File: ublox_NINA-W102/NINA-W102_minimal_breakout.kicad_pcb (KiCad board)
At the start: 2 copper layers, 16 parts, among them J1 Conn_01x15, J2 Conn_01x15, J3 6_PIN_SERIAL_TARGETLOCK, SW1 BOOT, SW2 RESET, U1 NINA-W102

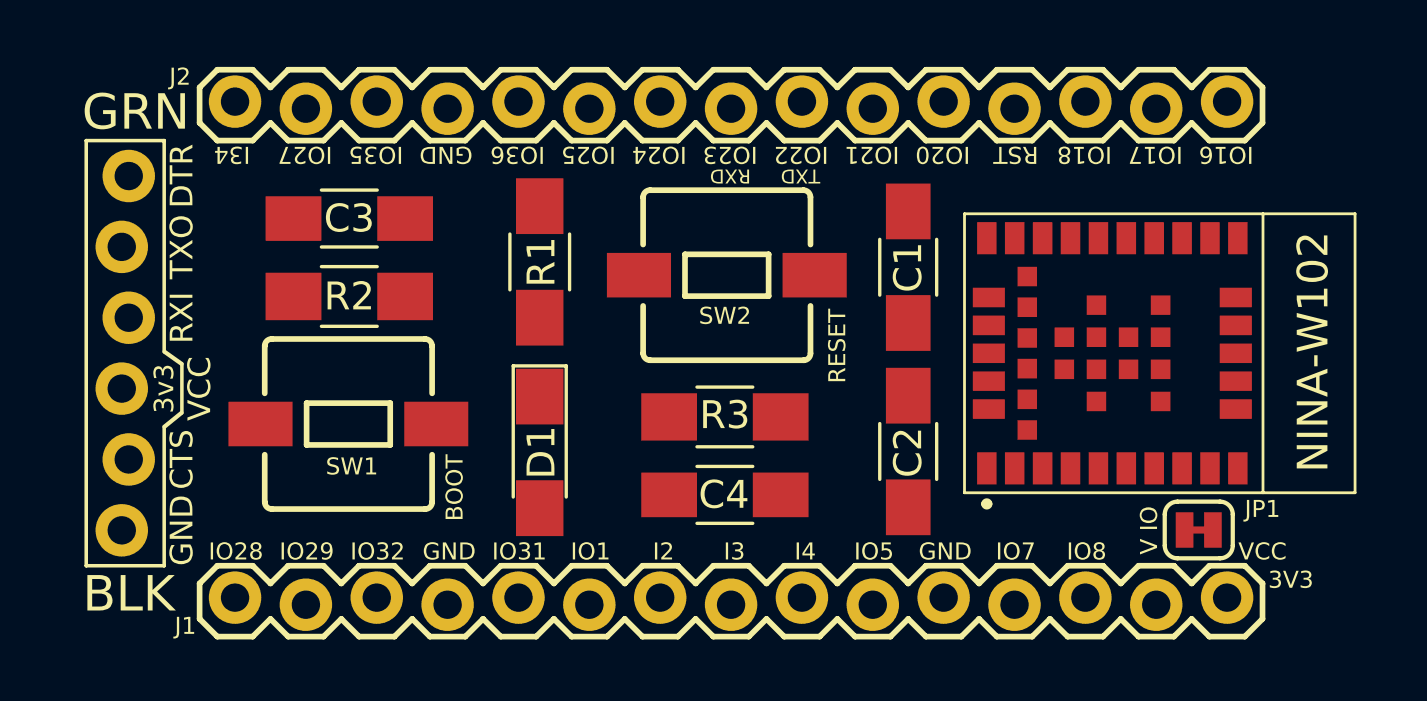
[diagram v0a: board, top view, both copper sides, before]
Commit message: First routing done
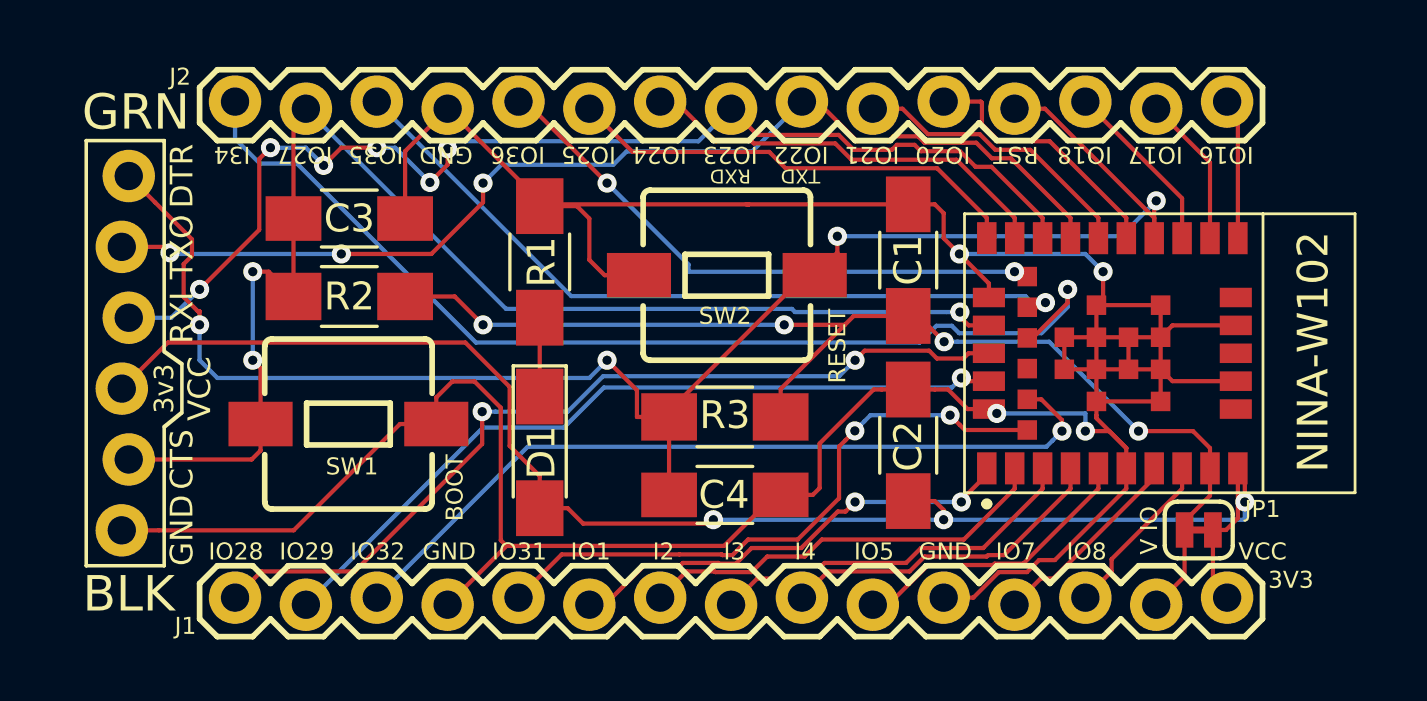
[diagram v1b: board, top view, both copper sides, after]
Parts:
- moved C1 0.25 mm to (134.6, 103.1)
- moved C2 0.22 mm to (134.6, 109.7)
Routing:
- net GND: track 0.00 -> 129.4 mm, vias 0 -> 4
- net DTR: track 0.00 -> 59.4 mm, vias 0 -> 4
- net +3V3: track 0.00 -> 55.1 mm, vias 0 -> 3
- net CTS: track 0.00 -> 47.9 mm, vias 0 -> 3
- net +1V8: track 0.00 -> 42.0 mm, vias 0 -> 4
- net RXD: track 0.00 -> 41.7 mm, vias 0 -> 6
- net TXD: track 0.00 -> 39.4 mm, vias 0 -> 3
- net Net-(J2-Pad1): track 0.00 -> 38.0 mm, vias 0 -> 1
- net Net-(J1-Pad1): track 0.00 -> 31.6 mm, vias 0 -> 2
- net Net-(J1-Pad3): track 0.00 -> 29.0 mm, vias 0 -> 1
- net Net-(J1-Pad2): track 0.00 -> 27.9 mm, vias 0 -> 1
- net Net-(J2-Pad3): track 0.00 -> 27.7 mm, vias 0 -> 1
- net Net-(J1-Pad5): track 0.00 -> 22.3 mm, vias 0 -> 2
- net Net-(J2-Pad5): track 0.00 -> 21.0 mm, vias 0 -> 2
- net Net-(J2-Pad6): track 0.00 -> 16.6 mm
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
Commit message: First try with groundplane
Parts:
- moved ? 10.5 mm to (83.7, 106.3)
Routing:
- added copper zone on B.Cu, net GND
- added copper zone on F.Cu, net GND
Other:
- board outline added: 47 x 20.7 mm

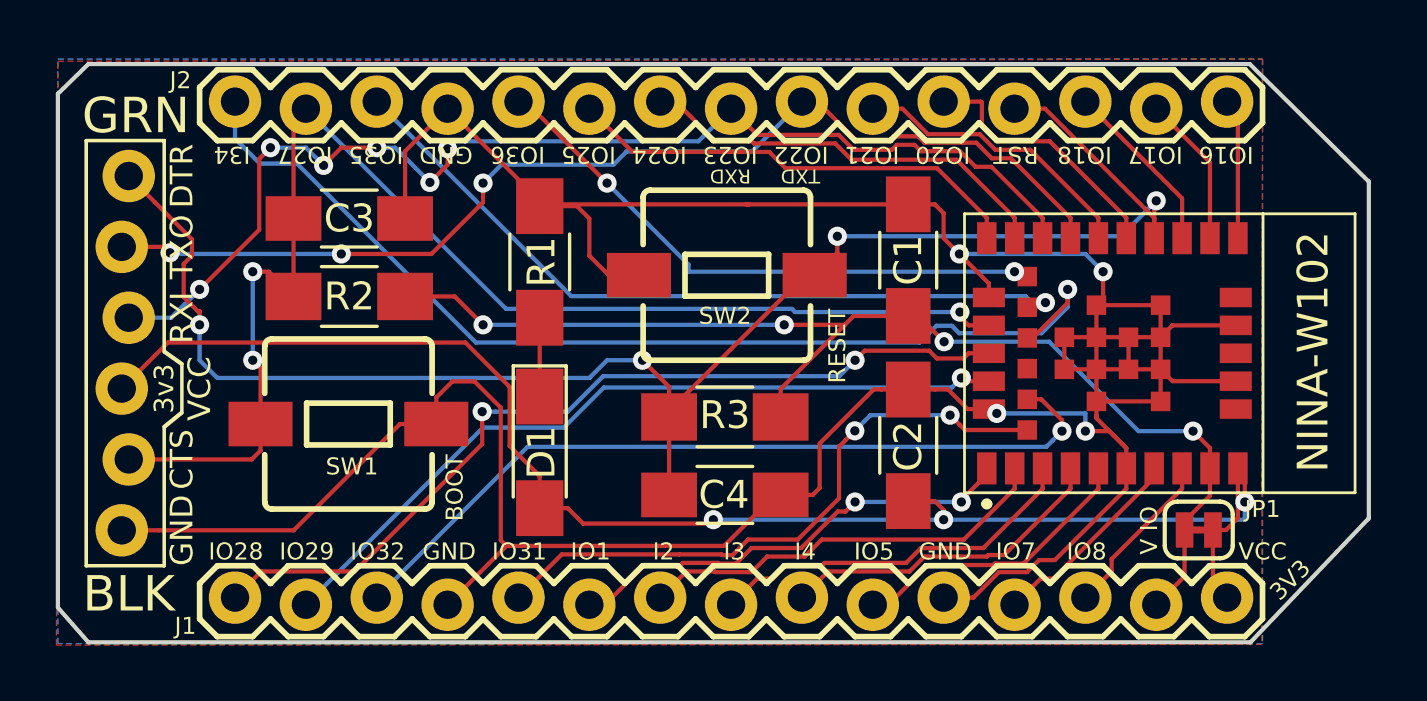
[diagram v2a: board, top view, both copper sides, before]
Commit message: Rerouting and thickening power tracks to 10mils, integrating some of the feedback from Michael
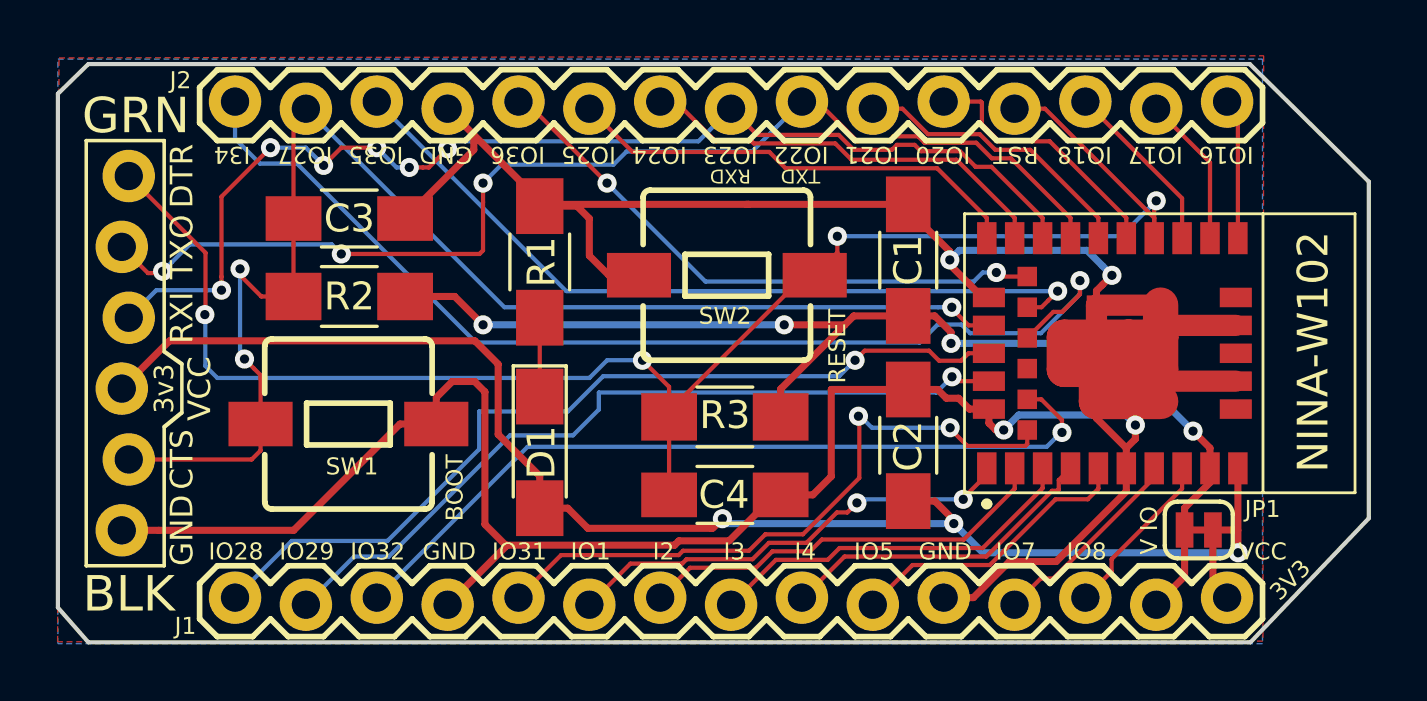
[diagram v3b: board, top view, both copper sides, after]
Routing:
- net GND: track 129.3 -> 131.5 mm
- net TXD: track 39.4 -> 41.2 mm
- net Net-(J2-Pad1): track 38.0 -> 39.1 mm
- net Net-(J1-Pad5): track 22.3 -> 23.2 mm
- net Net-(J2-Pad3): track 27.7 -> 28.5 mm
- net CTS: track 47.9 -> 48.8 mm
- net Net-(J1-Pad1): track 31.6 -> 31.7 mm, vias 2 -> 1

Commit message: Added some ground pad vias and corrected placement of problematic vias as feedback from Michael Ammann
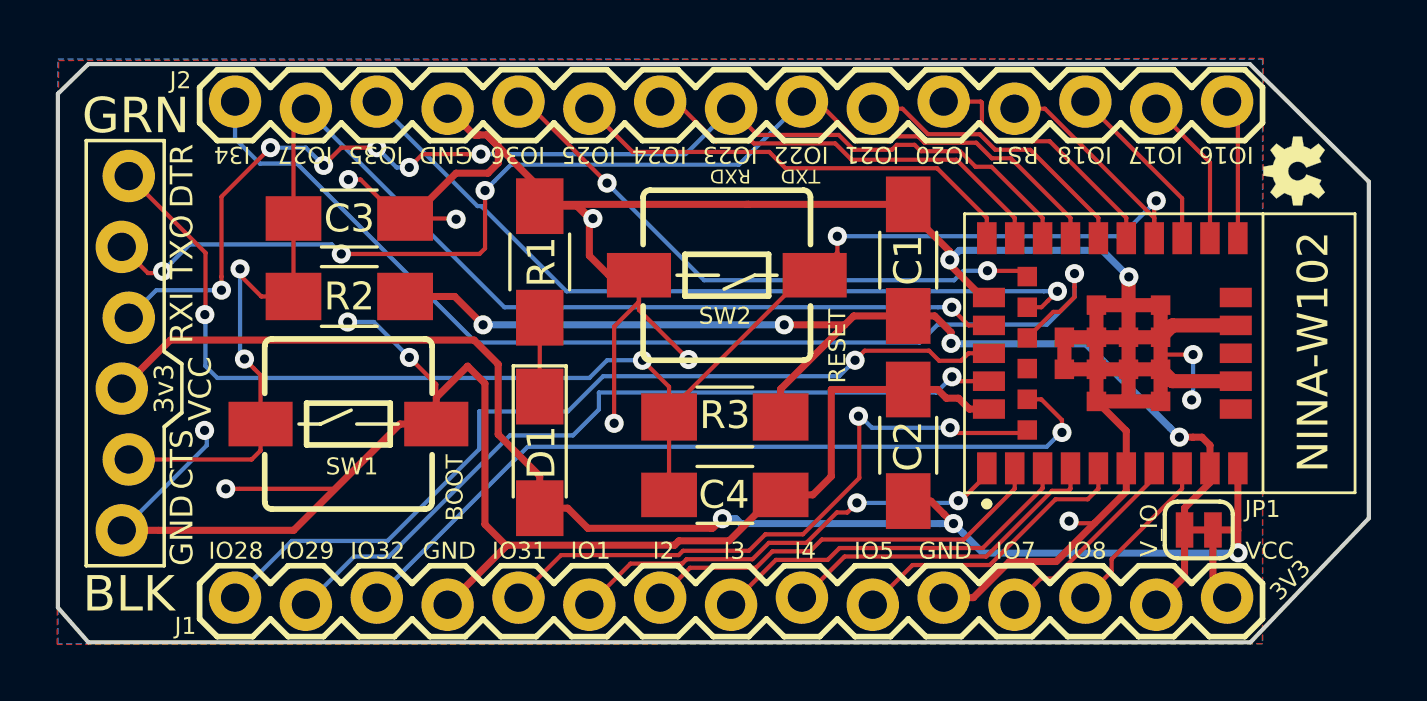
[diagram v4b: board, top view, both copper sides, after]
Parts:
- added ?: , Aesthetics:OSHW-LOGO-MINI, F.Cu at (148.6, 99.9)
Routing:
- net GND: track 131.5 -> 167.0 mm, vias 4 -> 14
- net Net-(J1-Pad5): track 23.2 -> 22.6 mm
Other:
- rule pad_to_mask_clearance: 0.2 -> 0.0508
- board text added: "V_IO"
- board text removed: "V IO"
